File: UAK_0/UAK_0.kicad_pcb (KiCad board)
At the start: 2 copper layers, 100 x 90 mm, 30 parts, among them X1 Крепежное_отверстие_d2, X2 Крепежное_отверстие_d2, X3 Крепежное_отверстие_d2, X4 Крепежное_отверстие_М3, X5 Крепежное_отверстие_М3, X6 Крепежное_отверстие_М3, X7 Крепежное_отверстие_М3, X8 Клеммник_х2_KLS2-300-5.00-02P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

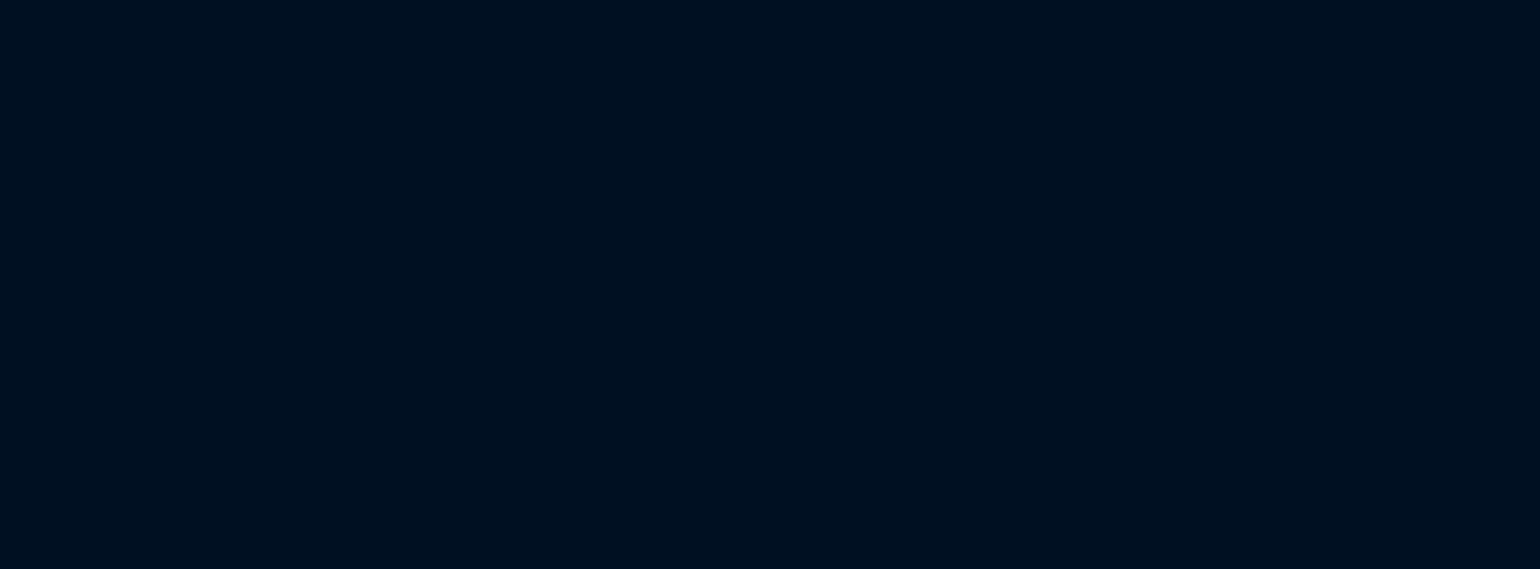
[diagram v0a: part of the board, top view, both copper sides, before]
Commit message: BOOT&PRG, концевик, ЖК, звук, подсветка - без трассировки
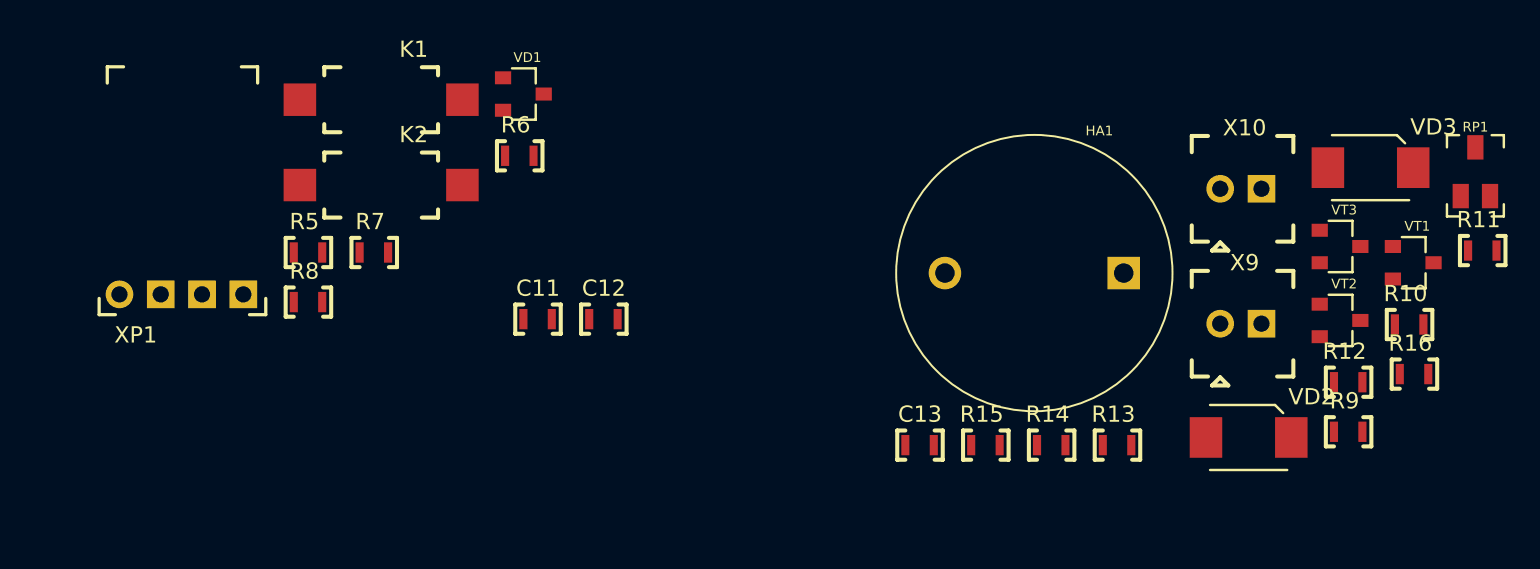
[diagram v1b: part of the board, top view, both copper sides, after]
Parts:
- added C11: Конденсатор_керамический, N_RLC:Конденсатор_SMD_0603, F.Cu at (141.2, 29.2)
- added C12: Конденсатор_керамический, N_RLC:Конденсатор_SMD_0603, F.Cu at (145.3, 29.2)
- added C13: Конденсатор_керамический, N_RLC:Конденсатор_SMD_0603, F.Cu at (164.8, 37.0)
- added HA1: Излучатель_HPA17F, N_VD_HL:Зуммер_HPA17F, F.Cu at (172.7, 26.4)
- added K1: Кнопка_FSMSM, N_X:Кнопка_FSMSM, F.Cu at (127.5, 15.8)
- added K2: Кнопка_FSMSM, N_X:Кнопка_FSMSM, F.Cu at (127.5, 21.0)
- added R10: Резистор_0,065Вт, N_RLC:Резистор_SMD_0603_0,065_Вт, F.Cu at (194.9, 29.6)
- added R11: Резистор_0,065Вт, N_RLC:Резистор_SMD_0603_0,065_Вт, F.Cu at (199.4, 25.0)
- added R12: Резистор_0,065Вт, N_RLC:Резистор_SMD_0603_0,065_Вт, F.Cu at (191.1, 33.1)
- added R13: Резистор_0,065Вт, N_RLC:Резистор_SMD_0603_0,065_Вт, F.Cu at (176.9, 37.0)
- added R14: Резистор_0,065Вт, N_RLC:Резистор_SMD_0603_0,065_Вт, F.Cu at (172.8, 37.0)
- added R15: Резистор_0,065Вт, N_RLC:Резистор_SMD_0603_0,065_Вт, F.Cu at (168.8, 37.0)
- added R16: Резистор_0,065Вт, N_RLC:Резистор_SMD_0603_0,065_Вт, F.Cu at (195.2, 32.6)
- added R5: Резистор_0,065Вт, N_RLC:Резистор_SMD_0603_0,065_Вт, F.Cu at (127.1, 25.1)
- added R6: Резистор_0,065Вт, N_RLC:Резистор_SMD_0603_0,065_Вт, F.Cu at (140.1, 19.2)
- added R7: Резистор_0,065Вт, N_RLC:Резистор_SMD_0603_0,065_Вт, F.Cu at (131.2, 25.1)
- added R8: Резистор_0,065Вт, N_RLC:Резистор_SMD_0603_0,065_Вт, F.Cu at (127.1, 28.2)
- added R9: Резистор_0,065Вт, N_RLC:Резистор_SMD_0603_0,065_Вт, F.Cu at (191.1, 36.2)
- added RP1: Резистор_подстроечный_PVA3A103, MOTOR_IMPORT_OTK:резистор_подстроечный_PVZ3A334, F.Cu at (199.8, 20.2)
- added VD1: Набор_диодов_BAR43CFILM, MOTOR_VD_VT_HL:Корпус_КТ-46, F.Cu at (141.2, 15.4)
- added VD2: Диод_шоттки_SK16, N_VD_HL:Диод_SMB, F.Cu at (183.5, 36.5)
- added VD3: Диод_шоттки_SK16, N_VD_HL:Диод_SMB, F.Cu at (191.0, 19.9)
- added VT1: Транзистор_полевой_N-канальный_IRLML6344TR, MOTOR_VD_VT_HL:Корпус_КТ-46, F.Cu at (196.0, 25.8)
- added VT2: Транзистор_полевой_N-канальный_IRLML6344TR, MOTOR_VD_VT_HL:Корпус_КТ-46, F.Cu at (191.5, 29.3)
- added VT3: Транзистор_полевой_N-канальный_IRLML6344TR, MOTOR_VD_VT_HL:Корпус_КТ-46, F.Cu at (191.5, 24.8)
- added X10: Клеммник_х2_308-021-14, N_X:Клеммник_х2_шаг2.54, F.Cu at (184.1, 21.2)
- added X9: Клеммник_х2_308-021-14, N_X:Клеммник_х2_шаг2.54, F.Cu at (184.1, 29.5)
- added XP1: Вилка_WF-4R, MOTOR_X:Вилка_СНП389-4ВП32-1-1, F.Cu at (116.4, 27.7)
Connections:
- net /SUPPLY_POWER/12V renamed /12V
- A1 pad 1: Net-(A1-Pad1) -> /DOOR_2
- A1 pad 14: Net-(A1-Pad14) -> /BUZZER
- A1 pad 15: Net-(A1-Pad15) -> /DOOR_2
- A1 pad 16: Net-(A1-Pad16) -> /MC_OUT_1
- A1 pad 2: Net-(A1-Pad2) -> /3V3
- A1 pad 23: Net-(A1-Pad23) -> /DOOR_SENSOR
- A1 pad 25: Net-(A1-Pad25) -> /BOOT_SEL
- A1 pad 26: Net-(A1-Pad26) -> /LCD_DATA_7
- A1 pad 29: Net-(A1-Pad29) -> /LCD_DATA_5
- A1 pad 3: Net-(A1-Pad3) -> /EN_RESET
- A1 pad 30: Net-(A1-Pad30) -> /LCD_E
- A1 pad 31: Net-(A1-Pad31) -> /LCD_A0
- A1 pad 33: Net-(A1-Pad33) -> /LCD_DATA_4
- A1 pad 34: Net-(A1-Pad34) -> /BOOT_UART_RX
- A1 pad 35: Net-(A1-Pad35) -> /BOOT_UART_TX
- A1 pad 36: Net-(A1-Pad36) -> /LCD_DATA_6
- A1 pad 37: Net-(A1-Pad37) -> /LCD_LED
- A1 pad 38: Net-(A1-Pad38) -> /DOOR_2
- A1 pad 39: Net-(A1-Pad39) -> /DOOR_2
- C1 pad 2: /SUPPLY_POWER/GND -> /DOOR_2
- C10 pad 1: /SUPPLY_POWER/3V3 -> /3V3
- C10 pad 2: /SUPPLY_POWER/GND -> /DOOR_2
- C2 pad 2: /SUPPLY_POWER/GND -> /DOOR_2
- C3 pad 2: /SUPPLY_POWER/GND -> /DOOR_2
- C7 pad 1: /SUPPLY_POWER/5V -> /5V
- C7 pad 2: /SUPPLY_POWER/GND -> /DOOR_2
- C8 pad 2: /SUPPLY_POWER/GND -> /DOOR_2
- C9 pad 1: /SUPPLY_POWER/5V -> /5V
- C9 pad 2: /SUPPLY_POWER/GND -> /DOOR_2
- DD1 pad 4: /SUPPLY_POWER/GND -> /DOOR_2
- G2 pad 1: /SUPPLY_POWER/GND -> /DOOR_2
- G2 pad 2: /SUPPLY_POWER/3V3 -> /3V3
- G2 pad 3: /SUPPLY_POWER/5V -> /5V
- HL1 pad 1: Net-(HL1-Pad1) -> /DOOR_2
- HL1 pad 11: Net-(HL1-Pad11) -> /LCD_DATA_4
- HL1 pad 12: Net-(HL1-Pad12) -> /LCD_DATA_5
- HL1 pad 13: Net-(HL1-Pad13) -> /LCD_DATA_6
- HL1 pad 14: Net-(HL1-Pad14) -> /LCD_DATA_7
- HL1 pad 15: Net-(HL1-Pad15) -> /5V
- HL1 pad 2: Net-(HL1-Pad2) -> /5V
- HL1 pad 4: Net-(HL1-Pad4) -> /LCD_A0
- HL1 pad 5: Net-(HL1-Pad5) -> /DOOR_2
- HL1 pad 6: Net-(HL1-Pad6) -> /LCD_E
- L1 pad 1: /SUPPLY_POWER/5V -> /5V
- L2 pad 3: /SUPPLY_POWER/GND -> /DOOR_2
- R3 pad 1: /SUPPLY_POWER/5V -> /5V
- R4 pad 2: /SUPPLY_POWER/GND -> /DOOR_2
- X2 pad 1: /SUPPLY_POWER/GND -> /DOOR_2
- X3 pad 1: /SUPPLY_POWER/5V -> /5V

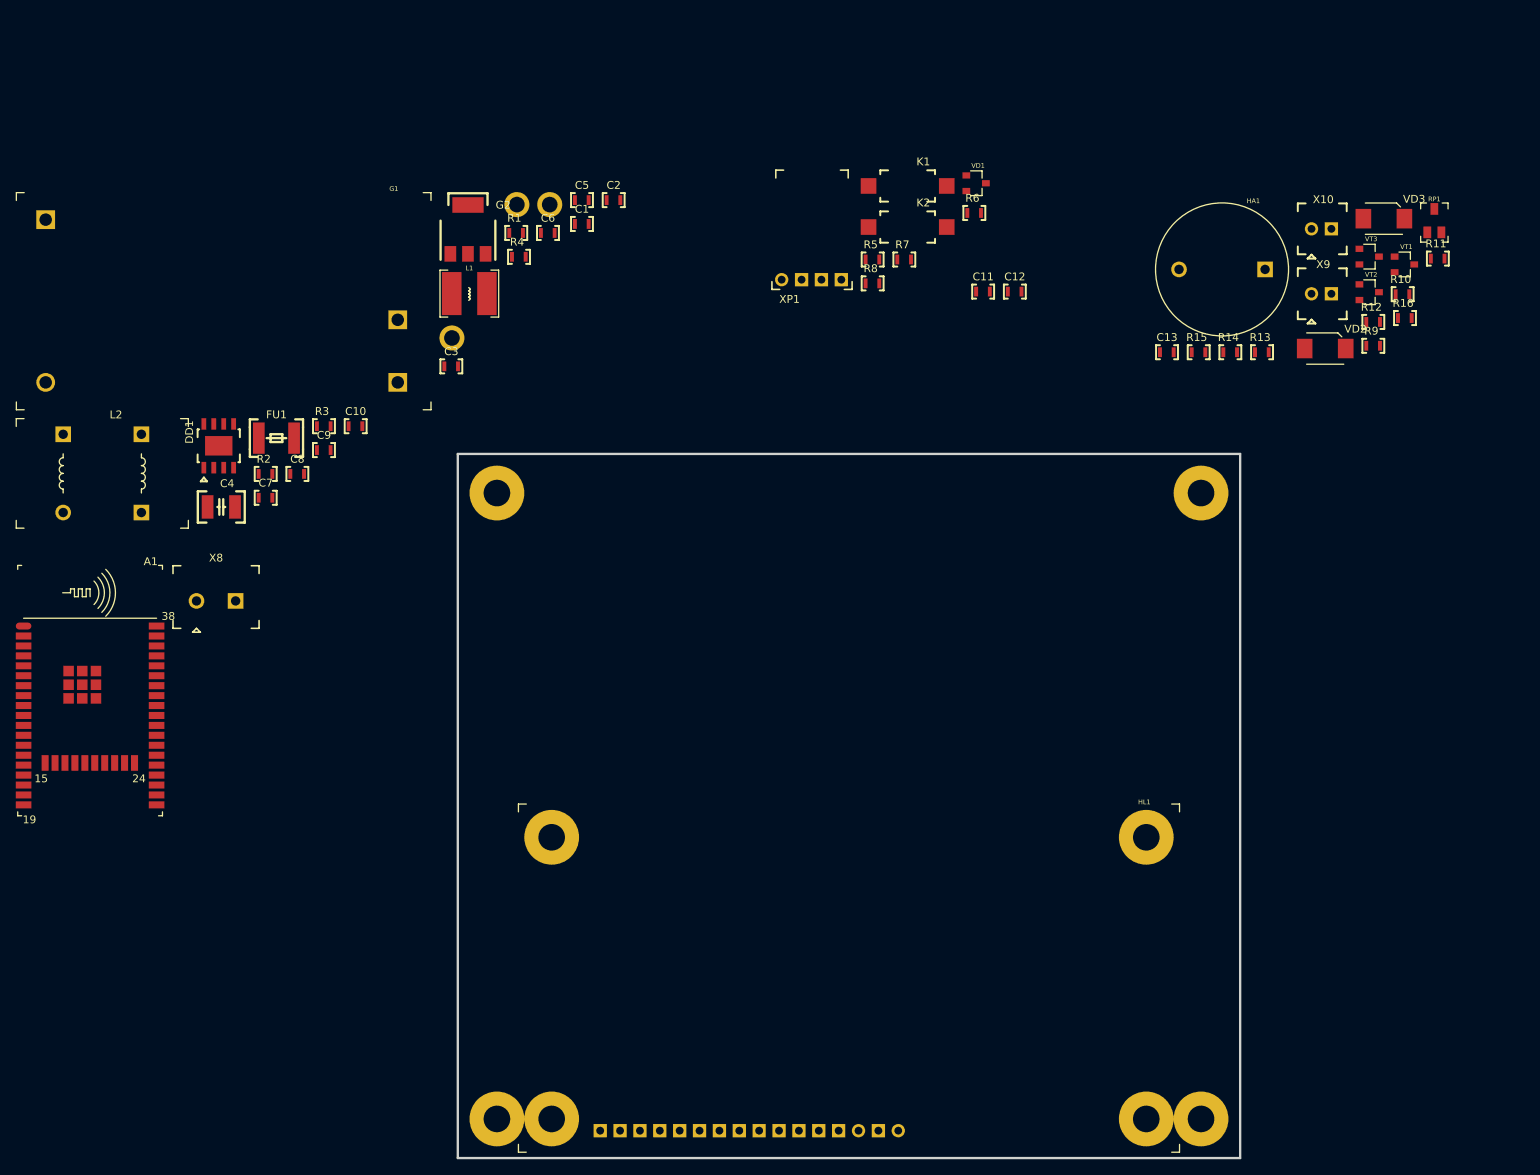
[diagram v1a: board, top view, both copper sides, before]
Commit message: нет коммутации 220В, остальная схема есть, нет трассировка
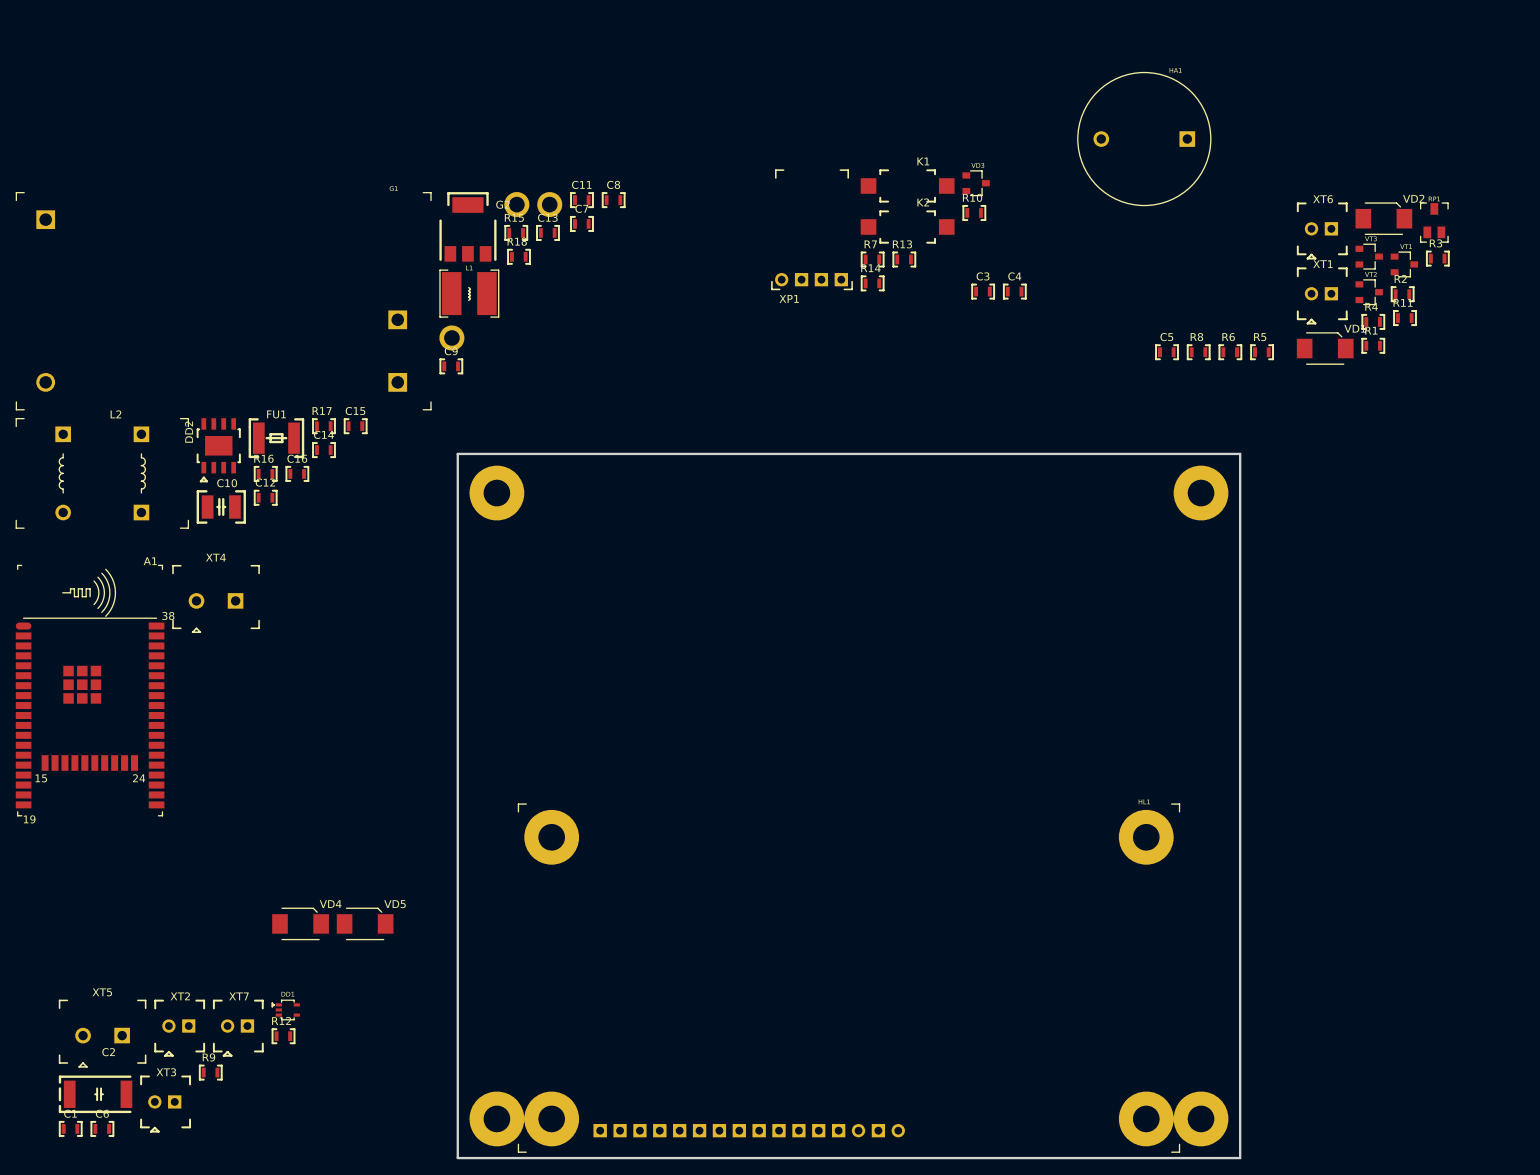
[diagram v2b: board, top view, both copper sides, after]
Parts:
- added C1: Конденсатор_керамический, N_RLC:Конденсатор_SMD_0603, F.Cu at (24.6, 136.3)
- added C2: Конденсатор_К53-56А-32В-22_мкФ+-10проц., MOTOR_RLC:Конденсатор_тантал_SMD_m7343, F.Cu at (25.4, 131.9)
- added C6: Конденсатор_керамический, N_RLC:Конденсатор_SMD_0603, F.Cu at (28.7, 136.3)
- added DD1: Повторитель_M74VHC1GT125, N_DD:SC-70-5, F.Cu at (53.3, 121.1)
- added R12: Резистор_0,065Вт, N_RLC:Резистор_SMD_0603_0,065_Вт, F.Cu at (51.8, 124.4)
- added R9: Резистор_0,065Вт, N_RLC:Резистор_SMD_0603_0,065_Вт, F.Cu at (42.5, 129.1)
- added VD4: Диод_шоттки_SK16, N_VD_HL:Диод_SMB, F.Cu at (52.5, 110.1)
- added VD5: Диод_шоттки_SK16, N_VD_HL:Диод_SMB, F.Cu at (60.8, 110.1)
- added XT2: Клеммник_х2_308-021-14, N_X:Клеммник_х2_шаг2.54, F.Cu at (38.1, 123.1)
- added XT3: Клеммник_х2_308-021-14, N_X:Клеммник_х2_шаг2.54, F.Cu at (36.3, 132.8)
- added XT5: Клеммник_х2_KLS2-300-5.00-02P-2S, N_X:Клеммник_х2_шаг5, F.Cu at (27.1, 124.4)
- added XT7: Клеммник_х2_308-021-14, N_X:Клеммник_х2_шаг2.54, F.Cu at (45.6, 123.1)
- moved HA1 19.4 mm to (162.8, 9.75)
- renumbered C4 to C10, C5 to C11, C7 to C12, C6 to C13, C9 to C14, C10 to C15, C8 to C16, C11 to C3, C12 to C4, C13 to C5, C1 to C7, C2 to C8, C3 to C9, DD1 to DD2, R9 to R1, R6 to R10, R16 to R11, R7 to R13, R8 to R14, R1 to R15, R2 to R16, R3 to R17, R4 to R18, R10 to R2, R11 to R3, R12 to R4, R13 to R5, R14 to R6, R5 to R7, R15 to R8, VD2 to VD1, VD3 to VD2, VD1 to VD3, X4 to X1, X6 to X2, X5 to X3, X7 to X4, X1 to X5, X2 to X6, X3 to X7, X9 to XT1, X8 to XT4, X10 to XT6
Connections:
- net Net-(C6-Pad2) renamed /0V_RES
- A1 pad 1: /DOOR_2 -> /BUTT_2
- A1 pad 11: Net-(A1-Pad11) -> /MC_OUT_1
- A1 pad 12: Net-(A1-Pad12) -> /EXT_BUTTON
- A1 pad 14: /BUZZER -> Net-(A1-Pad14)
- A1 pad 15: /DOOR_2 -> /BUTT_2
- A1 pad 16: /MC_OUT_1 -> /LCD_LED
- A1 pad 23: /DOOR_SENSOR -> /LCD_A0
- A1 pad 24: Net-(A1-Pad24) -> /LCD_E
- A1 pad 26: /LCD_DATA_7 -> /LCD_DATA_4
- A1 pad 30: /LCD_E -> /LCD_DATA_6
- A1 pad 31: /LCD_A0 -> /LCD_DATA_7
- A1 pad 33: /LCD_DATA_4 -> /BUZZER
- A1 pad 36: /LCD_DATA_6 -> /LED_WS2812
- A1 pad 37: /LCD_LED -> /DOOR_SENSOR
- A1 pad 38: /DOOR_2 -> /BUTT_2
- A1 pad 39: /DOOR_2 -> /BUTT_2
- C12 pad 2: /DOOR_2 -> /BUTT_2
- C13 pad 1: Net-(C6-Pad1) -> Net-(C13-Pad1)
- C14 pad 2: /DOOR_2 -> /BUTT_2
- C15 pad 2: /DOOR_2 -> /BUTT_2
- C16 pad 2: /DOOR_2 -> /BUTT_2
- C3 pad 2: /DOOR_2 -> /BUTT_2
- C4 pad 2: /DOOR_2 -> /BUTT_2
- C5 pad 1: /DOOR_2 -> /BUTT_2
- C7 pad 2: /DOOR_2 -> /BUTT_2
- C8 pad 2: /DOOR_2 -> /BUTT_2
- C9 pad 2: /DOOR_2 -> /BUTT_2
- DD2 pad 4: /DOOR_2 -> /BUTT_2
- G1 pad +V: Net-(C6-Pad1) -> Net-(G1-Pad+V)
- G2 pad 1: /DOOR_2 -> /BUTT_2
- HL1 pad 1: /DOOR_2 -> /BUTT_2
- HL1 pad 10: Net-(HL1-Pad10) -> /BUTT_2
- HL1 pad 5: /DOOR_2 -> /BUTT_2
- HL1 pad 7: Net-(HL1-Pad7) -> /BUTT_2
- HL1 pad 8: Net-(HL1-Pad8) -> /BUTT_2
- HL1 pad 9: Net-(HL1-Pad9) -> /BUTT_2
- K1 pad 1: /DOOR_2 -> /BUTT_2
- K2 pad 1: /DOOR_2 -> /BUTT_2
- L2 pad 3: /DOOR_2 -> /BUTT_2
- L2 pad 6: Net-(C6-Pad1) -> Net-(C13-Pad1)
- R18 pad 2: /DOOR_2 -> /BUTT_2
- R4 pad 2: /DOOR_2 -> /BUTT_2
- R5 pad 2: /DOOR_2 -> /BUTT_2
- R6 pad 2: /DOOR_2 -> /BUTT_2
- RP1 pad 2: /DOOR_2 -> /BUTT_2
- RP1 pad 3: /DOOR_2 -> /BUTT_2
- VT1 pad 2: /DOOR_2 -> /BUTT_2
- VT2 pad 2: /DOOR_2 -> /BUTT_2
- VT3 pad 2: /DOOR_2 -> /BUTT_2
- X6 pad 1: /DOOR_2 -> /BUTT_2
- XP1 pad 4: /DOOR_2 -> /BUTT_2
- XT6 pad 2: /DOOR_2 -> /BUTT_2

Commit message: подготовлена схема UAK_0A
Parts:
- added C17: Конденсатор_керамический, N_RLC:Конденсатор_SMD_1210, F.Cu at (110.6, 3.75)
- added DA1: МОП-реле_КР293КП1Б, N_DD:DIP6, F.Cu at (202.2, 54.8)
- added FU2: Предохранитель, N_RLC:Предохранитель_SMD_1812, F.Cu at (110.5, -1.95)
- added R19: Резистор_0,065Вт, N_RLC:Резистор_SMD_0603_0,065_Вт, F.Cu at (103.9, 6.23)
- added R20: Резистор_0,065Вт, N_RLC:Резистор_SMD_0603_0,065_Вт, F.Cu at (117.1, 2.63)
- added R21: Резистор_0,065Вт, N_RLC:Резистор_SMD_0603_0,065_Вт, F.Cu at (117.1, 5.68)
- added R22: Резистор_0,25Вт, N_RLC:Резистор_SMD_1206-0,25_Вт, F.Cu at (97.9, 6.58)
- added VT4: Транзистор_полевой_N-канальный_IRLML6344TR, MOTOR_VD_VT_HL:Корпус_КТ-46, F.Cu at (119.0, -2.72)
- added XT8: Клеммник_х2_KLS2-300-5.00-02P-2S, N_X:Клеммник_х2_шаг5, F.Cu at (100.1, 0.10)
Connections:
- A1 pad 10: Net-(A1-Pad10) -> /MC_220_OUT
